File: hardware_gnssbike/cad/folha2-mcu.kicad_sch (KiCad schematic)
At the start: 7 parts, among them J201 Tag-Connect TC2030-NL, U201 MinewSemi ME54BS13

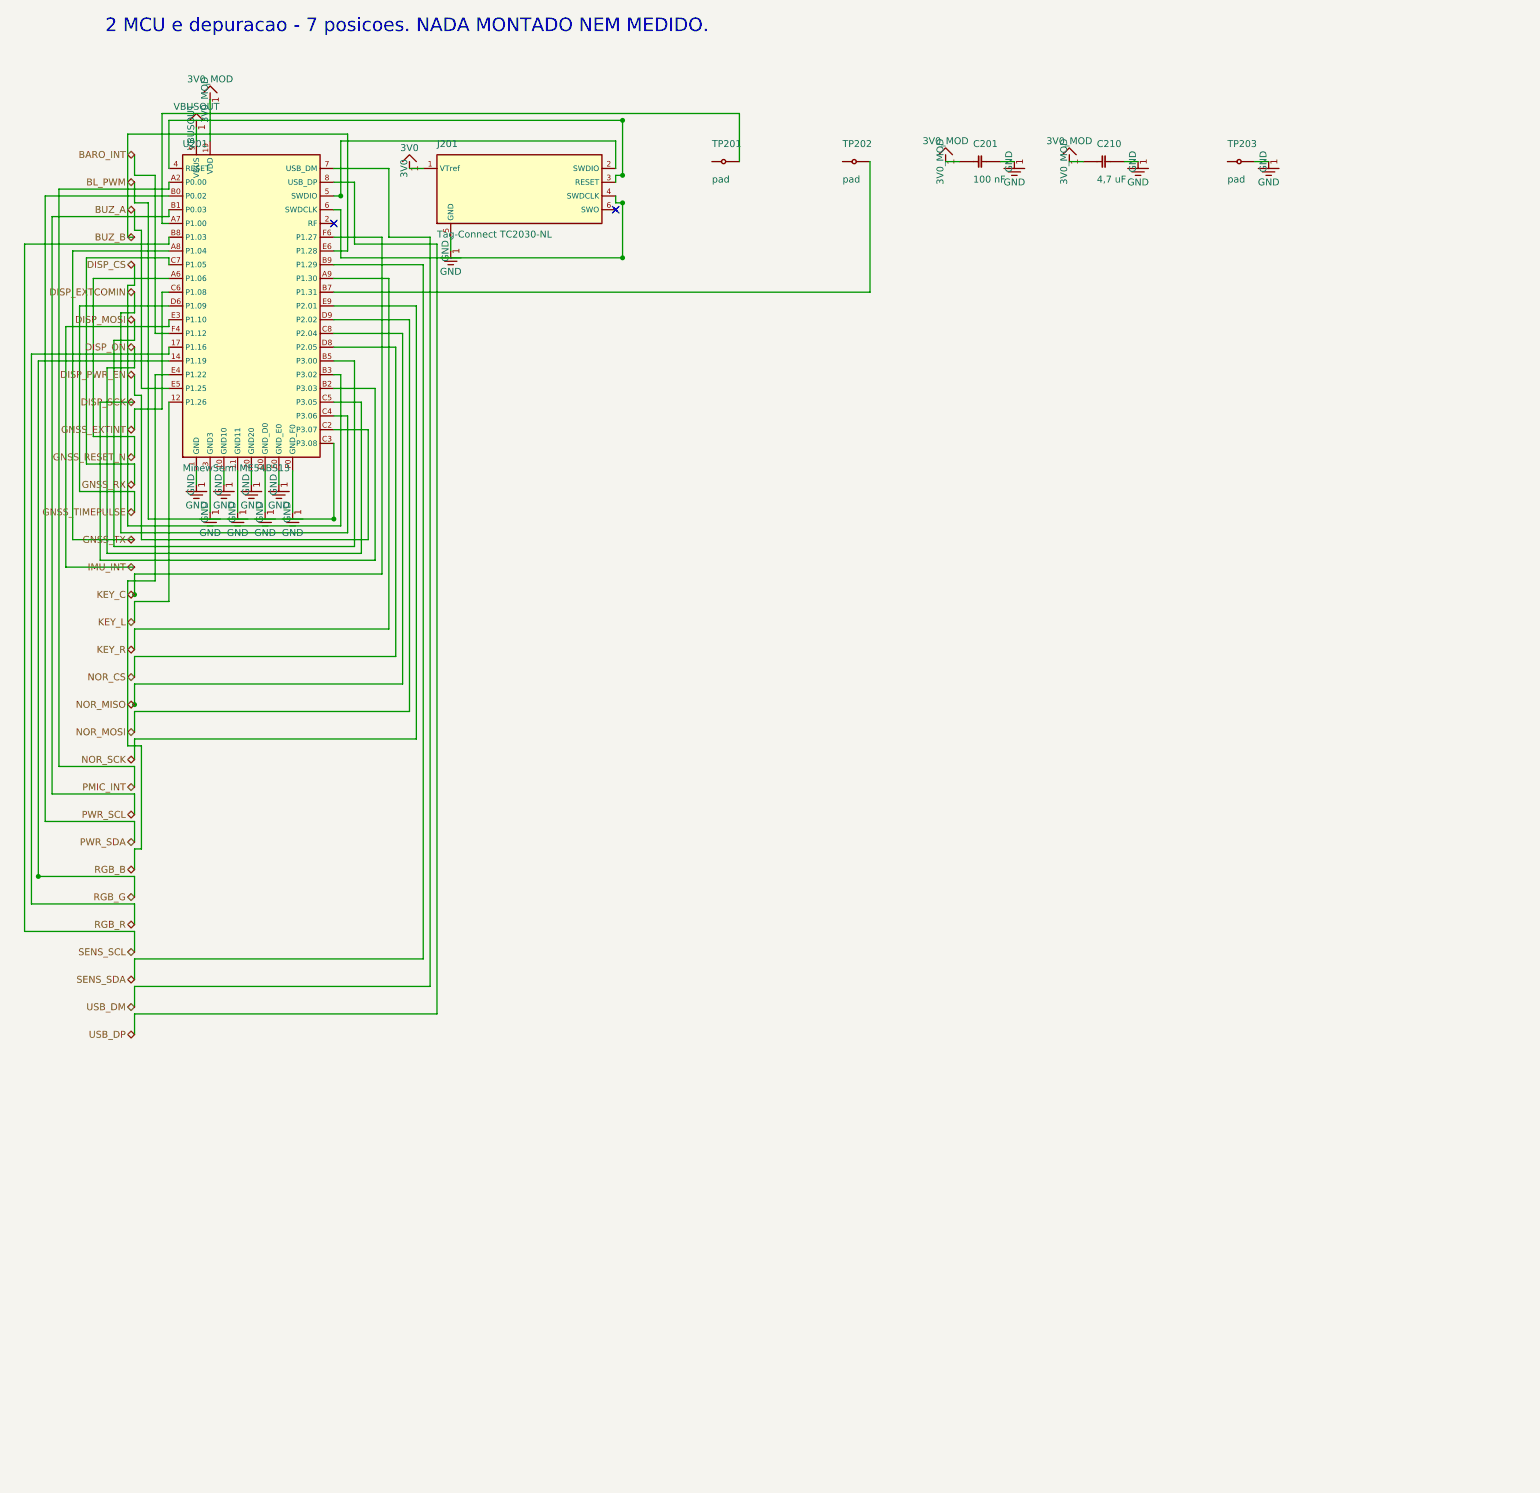
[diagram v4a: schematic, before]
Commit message: feat(hardware): draw the schematic by functional block, the way a person reads it
The owner asked for an industrial-standard schematic: wires and labels,
A4 or A3 pages, the right symbols and values, easy to read, the circuits
subdivided by dashed boxes. Until now each sheet was the netlist drawn as
wires - parts on a grid in connection order and a maze router pulling a
wire from every pin to wherever its other end was, across the page.

blocos.py turns each sheet into a row of functional blocks in the order
the signal flows, each in a dashed rectangle with a title: on the power
sheet, USB-C and protection, the nPM1300, the gauge and the cell, the GNSS
backup, the solar harvester, the thermal cut-off. Membership comes from
the BLOCOS table (the anchors), then make_pcb.DECOPLA and JUNTO (the
board already says whose each capacitor is), then sheets.SEGUE, then the
netlist without rails, nearest anchor by hops. Inside a block the anchor
sits in the middle and each passive beside the pin it serves, on the
side that pin faces, mirrored when the pin that serves the chip is the
far one; parts that touch only rails go to a shelf under the chip. Rails
are power symbols, neighbouring pins of one rail get a wire along their
tips and one symbol; a net that leaves its block is a local label, one
that leaves the sheet a hierarchical label, both on a short stub the
maze router bends when the straight way is taken. Sheet 1 is A3, the
rest A4, measured by the drawing itself. Decoupling capacitors now live
on their chip's sheet whatever their number.

Three KiCad 8 facts were measured with kicad-cli's netlist export on the
way, because the first version assumed each one wrong and check_sch.py
caught it: (mirror x) swaps left for right, not (mirror y); a local label
named after a rail is the net /sheet/RAIL, another net; and a pin in the
middle of a long wire is not on it - "wires connect with other wires or
pins only if their ends coincide exactly" (Eeschema manual). The
conventions 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
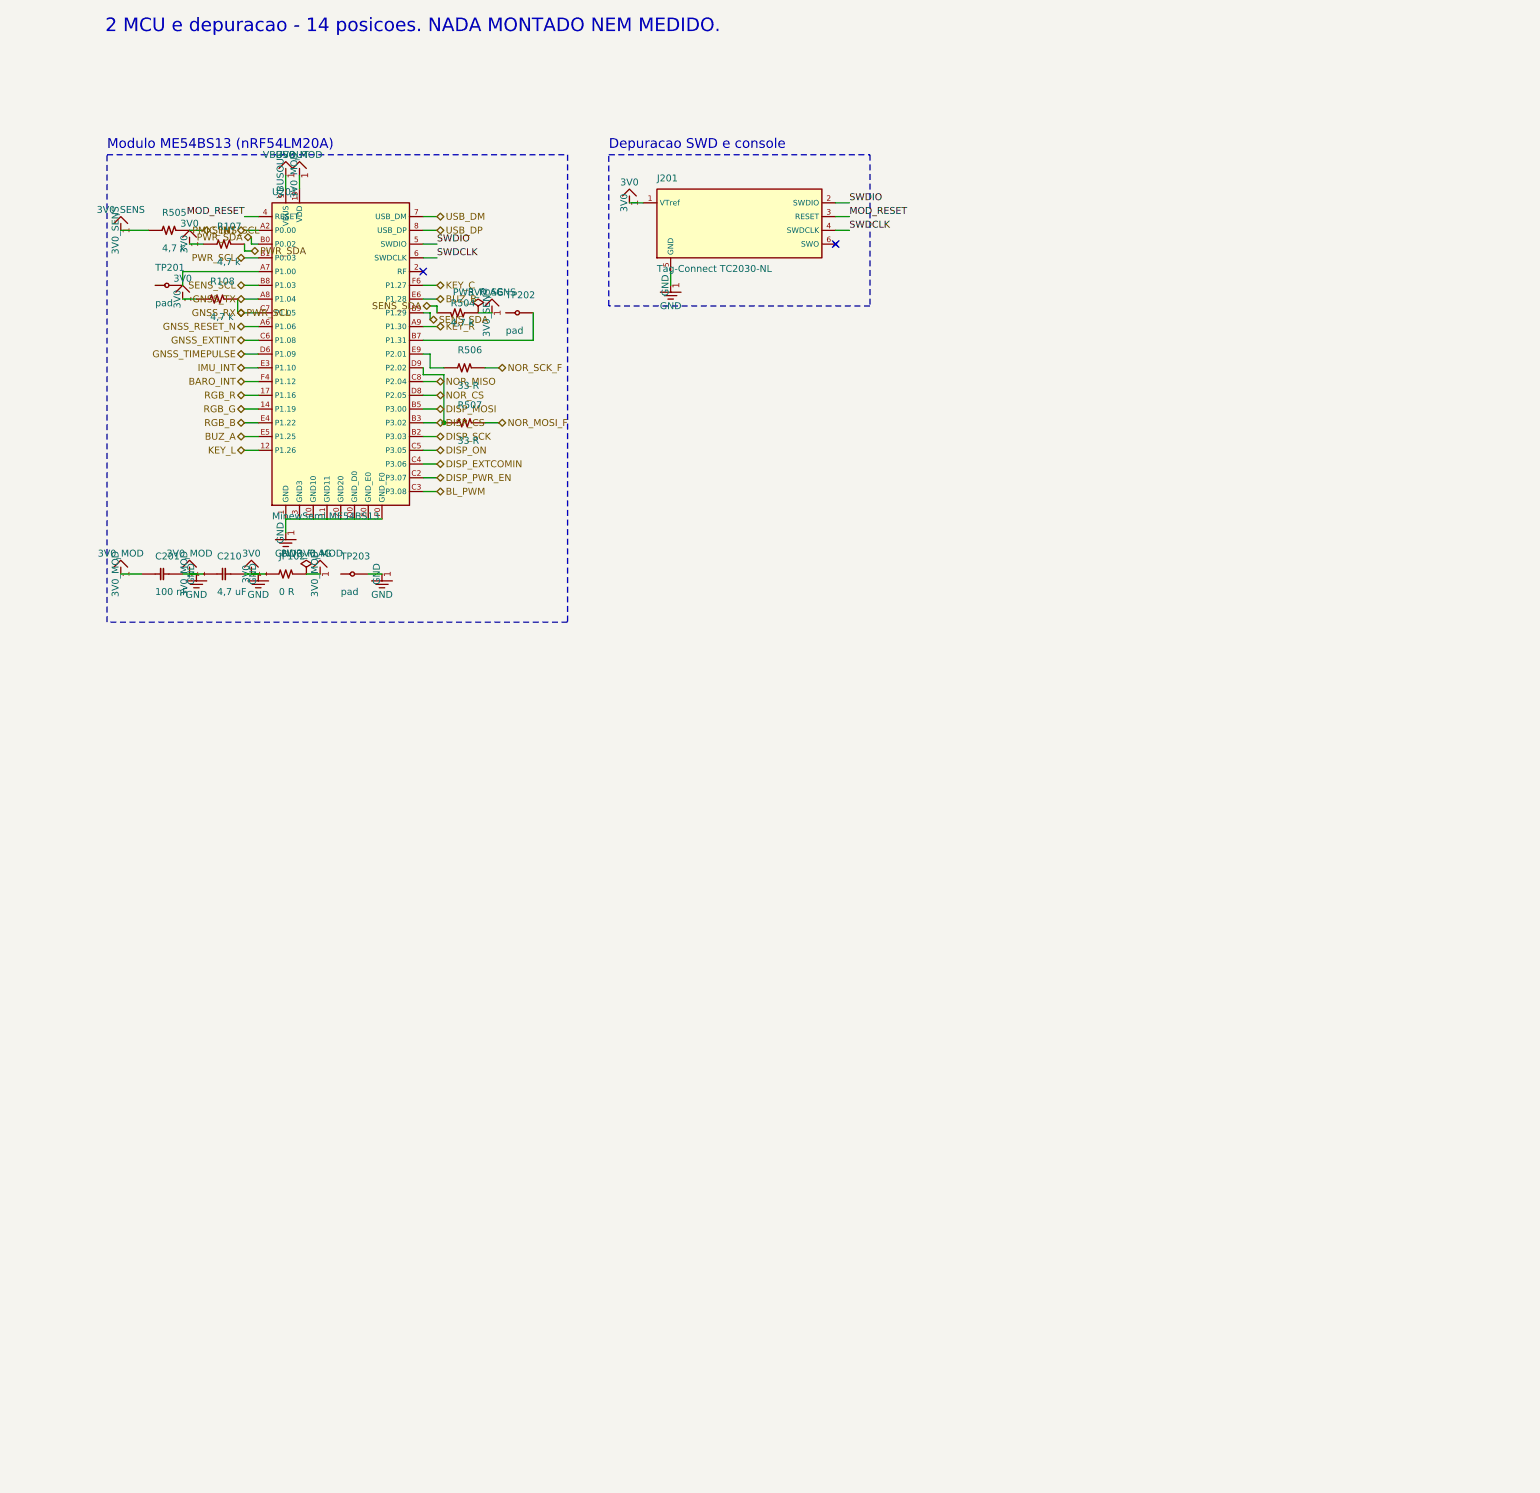
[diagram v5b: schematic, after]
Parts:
- added JP102: 0 R, Resistor_SMD:R_0402_1005Metric, symbol gnssbike:JP102
- added R107: 4,7 k, Resistor_SMD:R_0402_1005Metric, symbol gnssbike:R107
- added R108: 4,7 k, Resistor_SMD:R_0402_1005Metric, symbol gnssbike:R108
- added R504: 4,7 k, Resistor_SMD:R_0402_1005Metric, symbol gnssbike:R504
- added R505: 4,7 k, Resistor_SMD:R_0402_1005Metric, symbol gnssbike:R505
- added R506: 33 R, Resistor_SMD:R_0402_1005Metric, symbol gnssbike:R506
- added R507: 33 R, Resistor_SMD:R_0402_1005Metric, symbol gnssbike:R507
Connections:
- net 3V0_MOD is gone; now on net 3V0: C201.1, C210.1, U201.19 (VDD)
- net GND is gone; now on net 3V0: C201.2, C210.2, J201.5 (GND), TP203.1, U201.1 (GND), U201.10 (GND10), U201.11 (GND11), U201.20 (GND20), U201.3 (GND3), U201.D0 (GND_D0), U201.E0 (GND_E0), U201.F0 (GND_F0)
- net 3V0: now also JP102.1, JP102.2, R107.1, R108.1
- net PWR_SCL: now also R108.2
- net PWR_SDA: now also R107.2
- net SENS_SCL: now also R505.2
- net SENS_SDA: now also R504.2
- net MOD_RESET: now reaches J201.3 (RESET), U201.4 (RESET)
- net SWDIO: now reaches J201.2 (SWDIO), U201.5 (SWDIO)
- net SWDCLK: now reaches J201.4 (SWDCLK), U201.6 (SWDCLK)
- net NOR_MOSI: no longer names the net of U201.D9 (P2.02)
- net NOR_MOSI: now also R507.1
- net NOR_SCK: no longer names the net of U201.E9 (P2.01)
- net NOR_SCK: now also R506.1
- new net 3V0_SENS: R504.1, R505.1
- new net NOR_MOSI_F: R507.2
- new net NOR_SCK_F: R506.2
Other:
- note added: "2 MCU e depuracao - 14 posicoes. NADA MONTADO NEM MEDIDO."
- note added: "Depuracao SWD e console"
- note added: "Modulo ME54BS13 (nRF54LM20A)"
- note removed: "2 MCU e depuracao - 7 posicoes. NADA MONTADO NEM MEDIDO."
- moved on the sheet: C201, C210, J201, TP201, TP202, TP203, U201

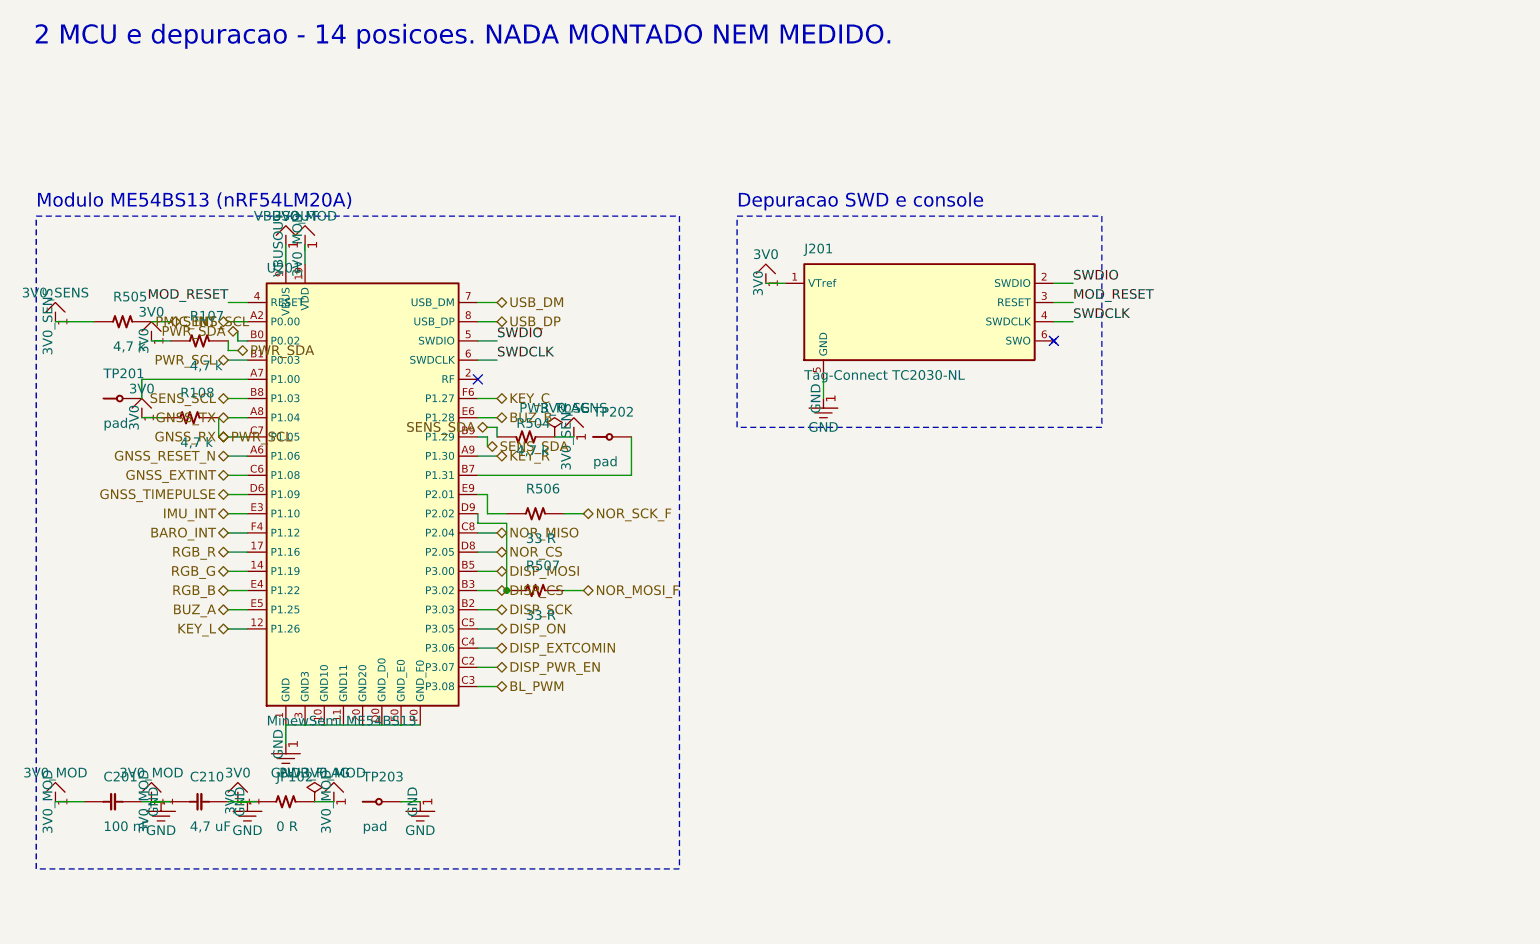
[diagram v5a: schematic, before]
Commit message: feat(hardware): spread the schematic so references, values and labels stay apart
The owner asked for the block-drawn schematic to be readable: designators
and labels were printing over each other. Power symbols now hide the pin
number and name (each printed a "1" and the rail's name twice) and point
away from their pin, lying along the line of a side pin with the name on
that line; the decoupling shelf is a row of stood-up capacitors per rail
with one wire along the tops and one symbol per row, test points standing
too; references and values sit to the right of a standing part and between
the neighbouring lines of a lying one, and block titles, part texts and
symbol names are obstacles for the router and for symbol and label
placement. Pull-ups and pull-downs of a labelled line stand past the label,
and off the corridor when the line goes on to another anchor; the labels'
room is reserved before the members are placed; the FPC connector is
mirrored to face the panel and aligned with it, its board-side wire
continuing from the label point, with the two nets of a pass-through pin
allowed to share cells; the two cells in front of every pin belong to its
net; DISP_VDD is drawn as a rail; blocks are packed by height and sheet 1
fits an A3.

The library symbol now always holds the base drawing and the instance
carries the rotation and mirror. The generator used to write the library
already flipped and the (mirror ...) token as well, applying the transform
twice, and the earlier "measurement" of (mirror x) was inverted by that.
Measured again on minimal files: (mirror y) swaps left for right, an
instance at 90 sends the left pin to the bottom, and KiCad transforms the
field justification along with the instance.

check_sch.py passes: the netlist equals nets.py pin by pin, no new ERC
error, no wire over a component. Eight nets are closed by labels where the
maze found no path inside the block, and the solar harvester and the left
of the gauge remain crowded; SCH_DEBUG=1 exp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
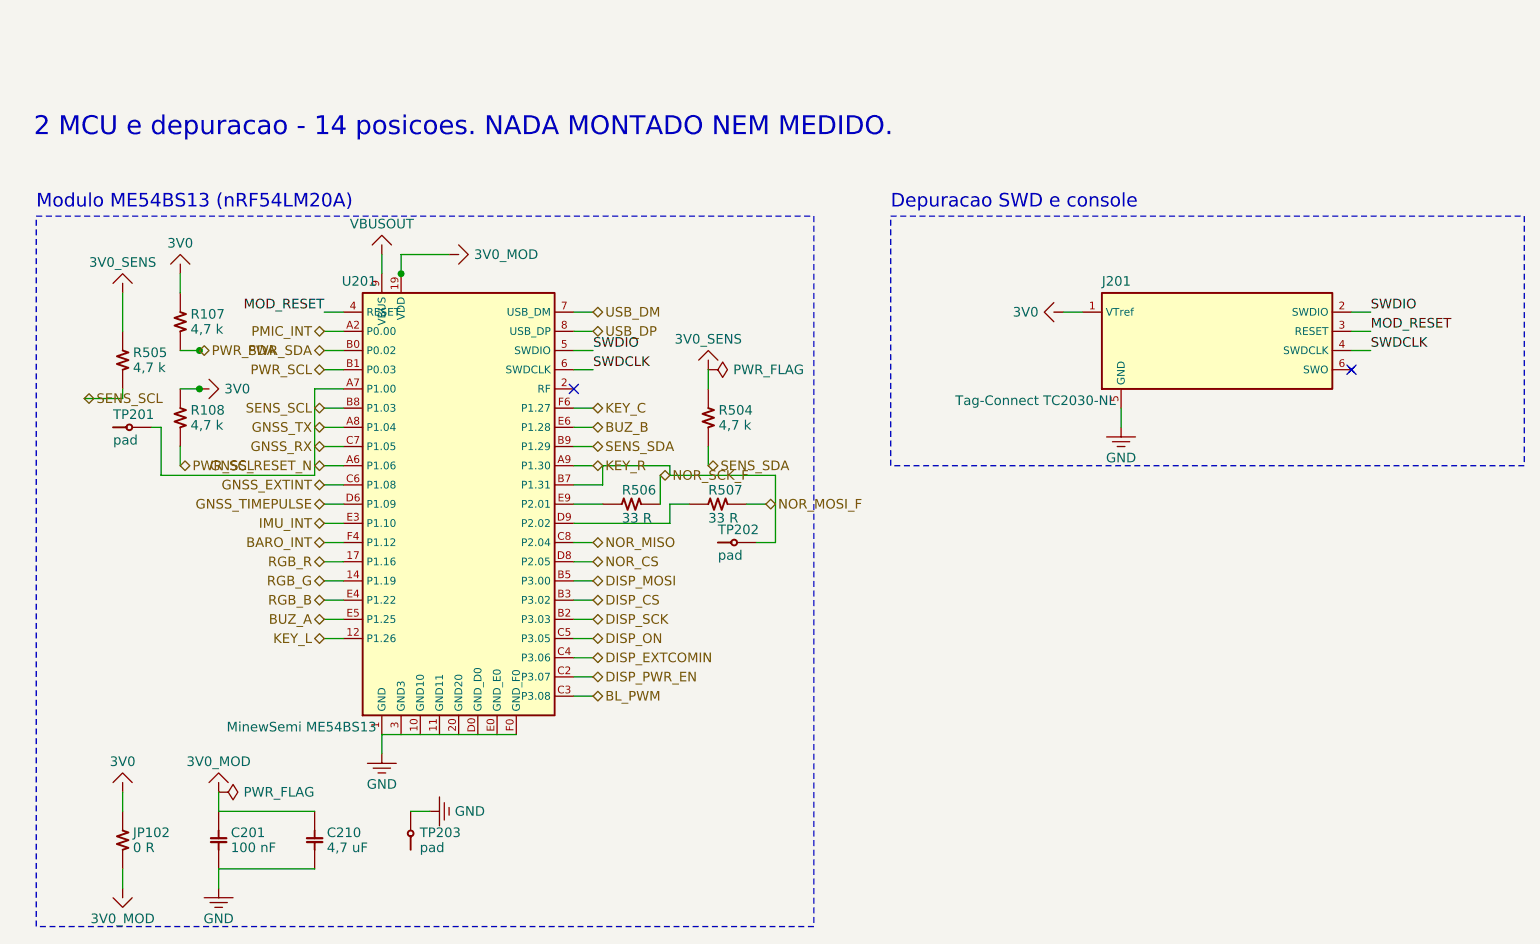
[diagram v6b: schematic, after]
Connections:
- net 3V0: no longer C201.1, C201.2, C210.1, C210.2, J201.5 (GND), JP102.2, TP203.1, U201.1 (GND), U201.10 (GND10), U201.11 (GND11), U201.19 (VDD), U201.20 (GND20), U201.3 (GND3), U201.D0 (GND_D0), U201.E0 (GND_E0), U201.F0 (GND_F0)
- new net 3V0_MOD: C201.1, C210.1, JP102.2, U201.19 (VDD)
- new net GND: C201.2, C210.2, J201.5 (GND), TP203.1, U201.1 (GND), U201.10 (GND10), U201.11 (GND11), U201.20 (GND20), U201.3 (GND3), U201.D0 (GND_D0), U201.E0 (GND_E0), U201.F0 (GND_F0)
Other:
- moved on the sheet: C201, C210, J201, JP102, R107, R108, R504, R505, R506, R507, TP201, TP202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
